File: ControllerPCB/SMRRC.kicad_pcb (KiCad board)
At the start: 2 copper layers, 58 x 58 mm, 27 parts, among them J1 Conn_01x08_Socket, J2 Conn_01x05, J3 Conn_01x03, J4 Conn_02x06_Odd_Even, SW1 SW_Push, SW2 SW_Push, U1 THVD1500, U2 PIC16F15345-I/SO, U3 L78L05_SOT89

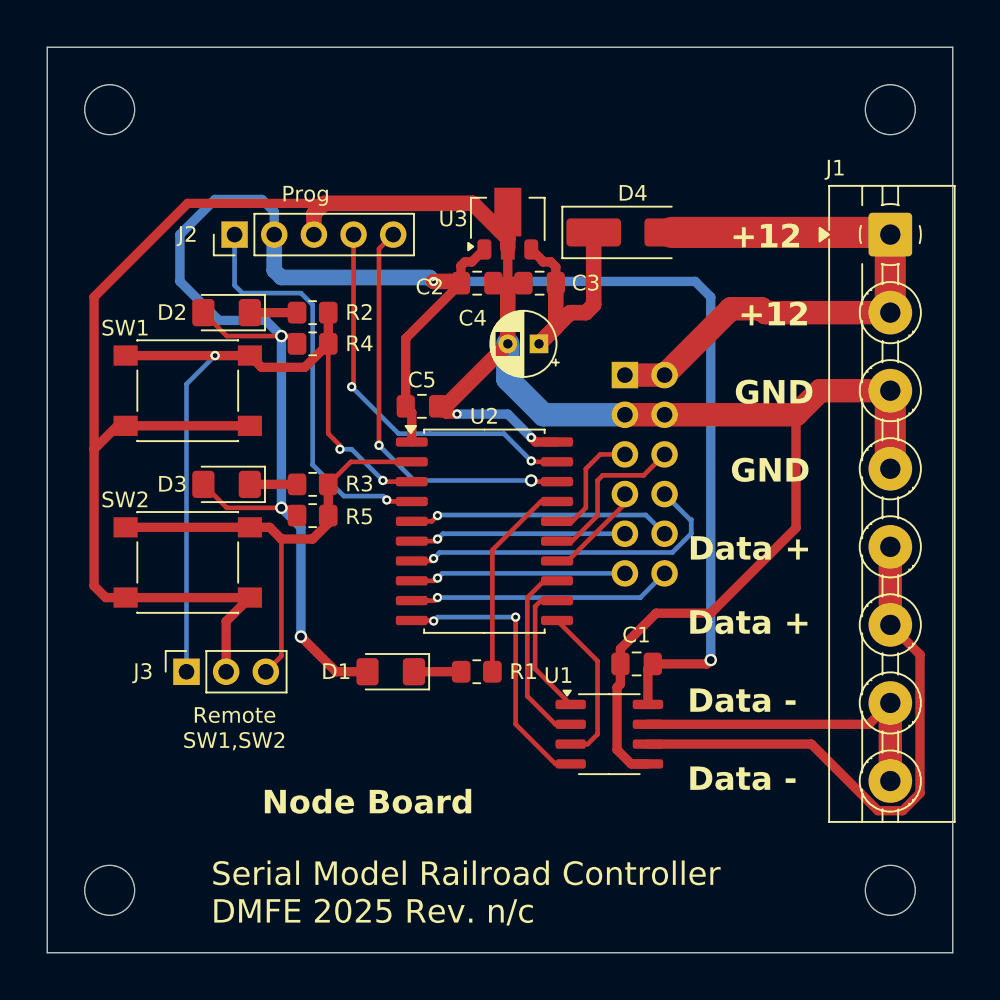
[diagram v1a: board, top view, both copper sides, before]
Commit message: Good test of USB to RS485
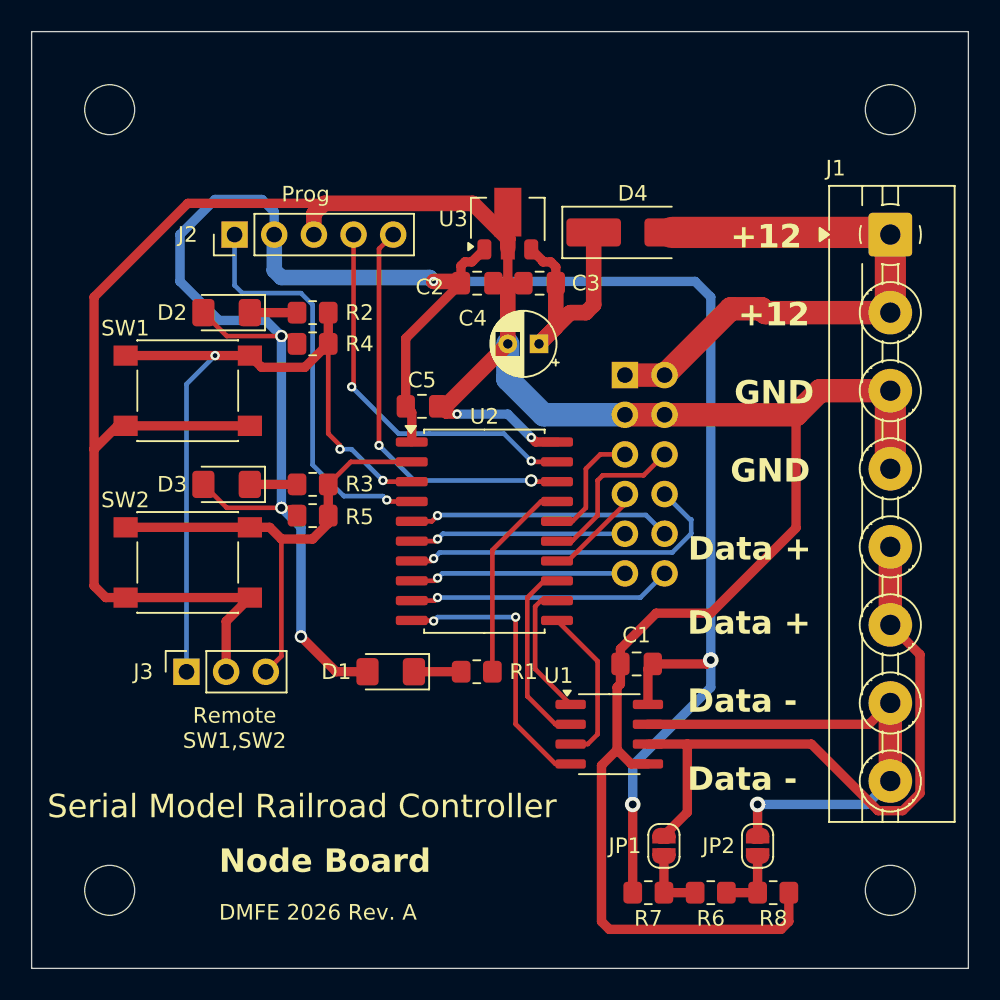
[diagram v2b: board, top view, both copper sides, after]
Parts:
- added JP1: Jumper_2_Open, Jumper:SolderJumper-2_P1.3mm_Open_RoundedPad1.0x1.5mm, F.Cu at (162.5, 89.2)
- added JP2: Jumper_2_Open, Jumper:SolderJumper-2_P1.3mm_Open_RoundedPad1.0x1.5mm, F.Cu at (168.5, 89.2)
- added R6: 120, Resistor_SMD:R_0805_2012Metric_Pad1.20x1.40mm_HandSolder, F.Cu at (165.5, 92.2)
- added R7: 10K, Resistor_SMD:R_0805_2012Metric_Pad1.20x1.40mm_HandSolder, F.Cu at (161.5, 92.2)
- added R8: 10K, Resistor_SMD:R_0805_2012Metric_Pad1.20x1.40mm_HandSolder, F.Cu at (169.5, 92.2)
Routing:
- net GND: track 164.3 -> 189.9 mm
- net +5V: track 135.7 -> 152.7 mm, vias 5 -> 6
- net Net-(J1-Pin_7): track 21.1 -> 32.2 mm, vias 0 -> 1
- net Net-(J1-Pin_5): track 36.2 -> 42.7 mm
- net Net-(JP2-B): track 0.00 -> 4.35 mm
- net Net-(JP1-B): track 0.00 -> 4.35 mm
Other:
- board size 58 x 58 mm -> 60 x 60 mm
- board text added: "DMFE 2026 Rev. A"
- board text added: "Serial Model Railroad Controller"
- board text removed: "Serial Model Railroad Controller DMFE 2025 Rev. n/c"
